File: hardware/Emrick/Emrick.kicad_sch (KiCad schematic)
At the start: 88 parts, among them J1 LED_STRIP_CONNECTOR, J2 UFL, J3 Conn_02x05_Odd_Even, J4 BATT_CONN, P1 USB_C_Plug_USB2.0, Q1 Q_NMOS_DGS, Q2 Q_NMOS_DGS, Q3 Q_NMOS_DGS, SW1 SW_SPST, SW2 SW_MEC_5E (RESET)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

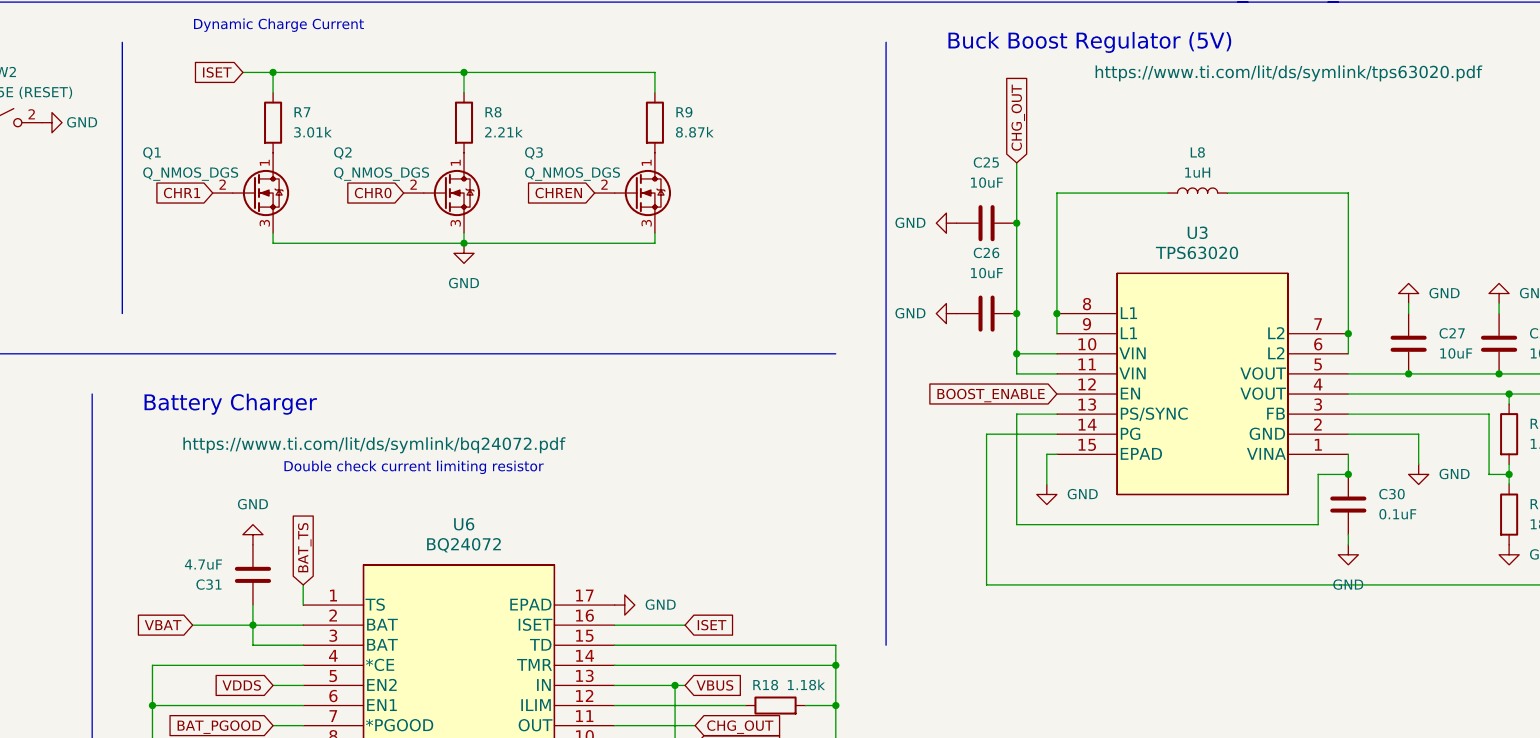
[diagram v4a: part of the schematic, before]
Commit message: switch NMOS to GSD and assign SOT-23 handsoldering footprint
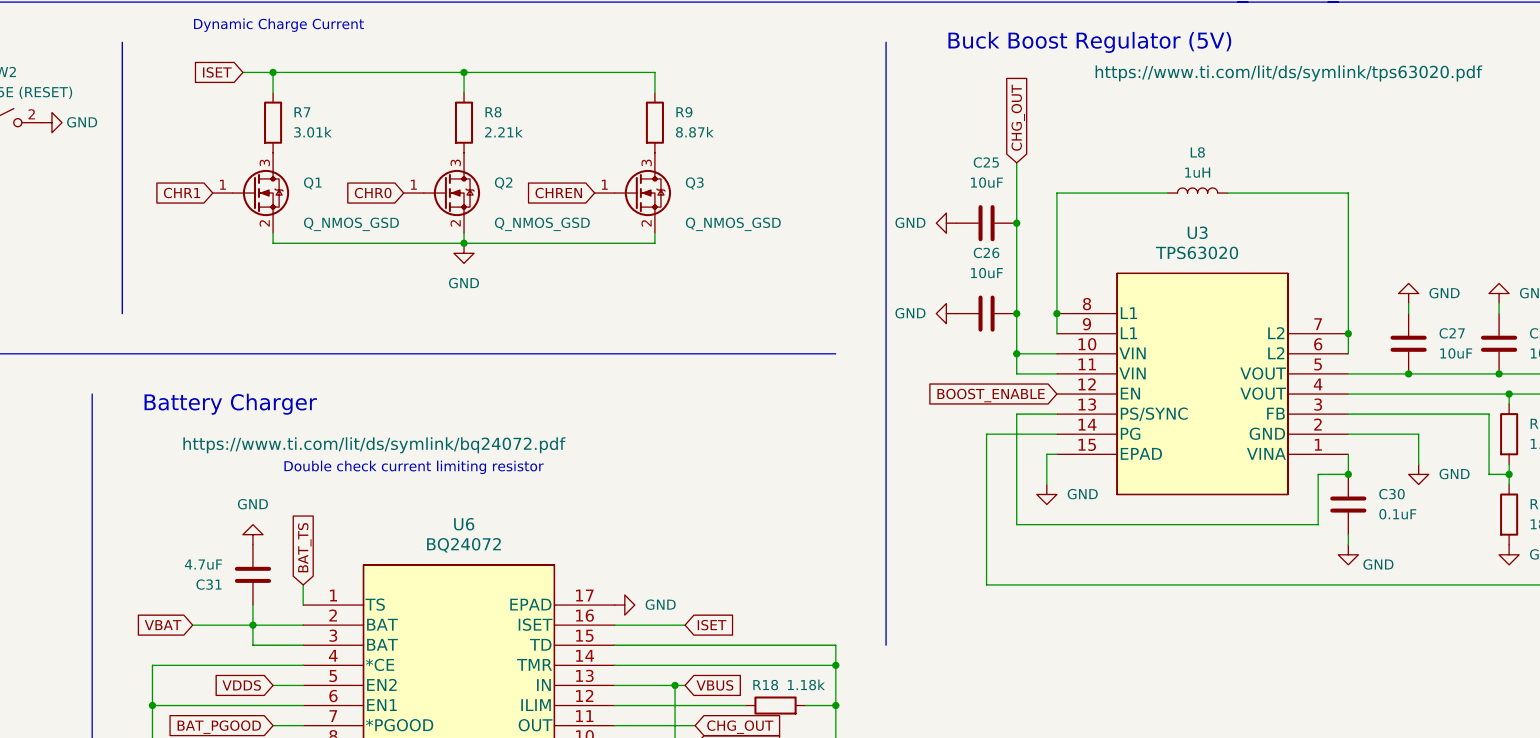
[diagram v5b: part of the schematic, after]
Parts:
- removed Q1, Q2, Q3: Q_NMOS_DGS, symbol Device:Q_NMOS_DGS
- added Q1, Q2, Q3: Q_NMOS_GSD, Package_TO_SOT_SMD:SOT-23_Handsoldering, symbol Device:Q_NMOS_GSD
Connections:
- net CHR0: now also Q2.1 (G)
- net CHR1: now also Q1.1 (G)
- net CHREN: now also Q3.1 (G)
- net GND: now also Q1.2 (S), Q2.2 (S), Q3.2 (S)
- net at R9.2: now also Q3.3 (D)
- net at R7.2: now also Q1.3 (D)
- net at R8.2: now also Q2.3 (D)
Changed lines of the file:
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@@
     (pin "2")
+  )
+  (symbol (lib_id "Device:Q_NMOS_GSD") (at 242.57 190.5 0) (unit 1)
+    (in_bom yes) (on_board yes)
+    (property "Reference" "Q2" (id 0) (at 248.92 189.2299 0)
+      (effects (font (size 1.27 1.27)) (justify left))
+    )
+    (property "Value" "Q_NMOS_GSD" (id 1) (at 248.92 194.31 0)
+      (effects (font (size 1.27 1.27)) (justify left))
+    )
+    (property "Footprint" "Package_TO_SOT_SMD:SOT-23_Handsoldering" (id 2) (at 247.65 187.96 0)
+      (effects (font (size 1.27 1.27)) hide)
+    )
+    (property "Datasheet" "~" (id 3) (at 242.57 190.5 0)
+      (effects (font (size 1.27 1.27)) hide)
+    )
+    (pin "1")
+    (pin "2")
+    (pin "3")
+  )
+  (symbol (lib_id "Device:Q_NMOS_GSD") (at 218.44 190.5 0) (unit 1)
+    (in_bom yes) (on_board yes)
+    (property "Reference" "Q1" (id 0) (at 224.79 189.2299 0)
+      (effects (font (size 1.27 1.27)) (justify left))
+    )
+    (property "Value" "Q_NMOS_GSD" (id 1) (at 224.79 194.31 0)
+      (effects (font (size 1.27 1.27)) (justify left))
+    )
+    (property "Footprint" "Package_TO_SOT_SMD:SOT-23_Handsoldering" (id 2) (at 223.52 187.96 0)
+      (effects (font (size 1.27 1.27)) hide)
+    )
+    (property "Datasheet" "~" (id 3) (at 218.44 190.5 0)
+      (effects (font (size 1.27 1.27)) hide)
+    )
+    (pin "1")
+    (pin "2")
+    (pin "3")
   )
   (symbol (lib_id "Device:FerriteBead") (at 336.55 36.83 90) (unit 1)
@@
     (pin "2")
   )
-  (symbol (lib_id "Device:Q_NMOS_DGS") (at 266.7 190.5 0) (unit 1)
-    (in_bom yes) (on_board yes)
-    (property "Reference" "Q3" (id 0) (at 252.73 185.42 0)
-      (effects (font (size 1.27 1.27)) (justify left))
-    )
-    (property "Value" "Q_NMOS_DGS" (id 1) (at 252.73 187.96 0)
-      (effects (font (size 1.27 1.27)) (justify left))
-    )
-    (property "Footprint" "" (id 2) (at 271.78 187.96 0)
-      (effects (font (size 1.27 1.27)) hide)
-    )
-    (property "Datasheet" "~" (id 3) (at 266.7 190.5 0)
-      (effects (font (size 1.27 1.27)) hide)
-    )
-    (pin "1")
-    (pin "2")
-    (pin "3")
-  )
   (symbol (lib_id "power:GND") (at 240.03 158.75 0) (unit 1)
     (in_bom yes) (on_board yes) (fields_autoplaced)
@@
     )
     (pin "1")
+  )
+  (symbol (lib_id "Device:Q_NMOS_GSD") (at 266.7 190.5 0) (unit 1)
+    (in_bom yes) (on_board yes)
+    (property "Reference" "Q3" (id 0) (at 273.05 189.2299 0)
+      (effects (font (size 1.27 1.27)) (justify left))
+    )
+    (property "Value" "Q_NMOS_GSD" (id 1) (at 273.05 194.31 0)
+      (effects (font (size 1.27 1.27)) (justify left))
+    )
+    (property "Footprint" "Package_TO_SOT_SMD:SOT-23_Handsoldering" (id 2) (at 271.78 187.96 0)
+      (effects (font (size 1.27 1.27)) hide)
+    )
+    (property "Datasheet" "~" (id 3) (at 266.7 190.5 0)
+      (effects (font (size 1.27 1.27)) hide)
+    )
+    (pin "1")
+    (pin "2")
+    (pin "3")
   )
   (symbol (lib_id "Device:Antenna") (at 339.09 113.03 0) (unit 1)
@@
     (pin "1")
     (pin "2")
-  )
-  (symbol (lib_id "Device:Q_NMOS_DGS") (at 242.57 190.5 0) (unit 1)
-    (in_bom yes) (on_board yes)
-    (property "Reference" "Q2" (id 0) (at 228.6 185.42 0)
-      (effects (font (size 1.27 1.27)) (justify left))
-    )
-    (property "Value" "Q_NMOS_DGS" (id 1) (at 228.6 187.96 0)
-      (effects (font (size 1.27 1.27)) (justify left))
-    )
-    (property "Footprint" "" (id 2) (at 247.65 187.96 0)
-      (effects (font (size 1.27 1.27)) hide)
-    )
-    (property "Datasheet" "~" (id 3) (at 242.57 190.5 0)
-      (effects (font (size 1.27 1.27)) hide)
-    )
-    (pin "1")
-    (pin "2")
-    (pin "3")
   )
   (symbol (lib_id "Device:C") (at 240.03 104.14 180) (unit 1)
@@
     (pin "2")
   )
-  (symbol (lib_id "Device:Q_NMOS_DGS") (at 218.44 190.5 0) (unit 1)
-    (in_bom yes) (on_board yes)
-    (property "Reference" "Q1" (id 0) (at 204.47 185.42 0)
-      (effects (font (size 1.27 1.27)) (justify left))
-    )
-    (property "Value" "Q_NMOS_DGS" (id 1) (at 204.47 187.96 0)
-      (effects (font (size 1.27 1.27)) (justify left))
-    )
-    (property "Footprint" "" (id 2) (at 223.52 187.96 0)
-      (effects (font (size 1.27 1.27)) hide)
-    )
-    (property "Datasheet" "~" (id 3) (at 218.44 190.5 0)
-      (effects (font (size 1.27 1.27)) hide)
-    )
-    (pin "1")
-    (pin "2")
-    (pin "3")
-  )
   (symbol (lib_id "Device:LED") (at 106.68 34.29 0) (unit 1)
     (in_bom yes) (on_board yes)
@@
   )
   (symbol (lib_id "power:GND") (at 356.87 234.95 0) (unit 1)
-    (in_bom yes) (on_board yes) (fields_autoplaced)
+    (in_bom yes) (on_board yes)
     (property "Reference" "#PWR039" (id 0) (at 356.87 241.3 0)
       (effects (font (size 1.27 1.27)) hide)
     )
-    (property "Value" "GND" (id 1) (at 356.87 240.03 0))
+    (property "Value" "GND" (id 1) (at 360.68 237.49 0))
     (property "Footprint" "" (id 2) (at 356.87 234.95 0)
       (effects (font (size 1.27 1.27)) hide)
@@
       (reference "P1") (unit 1) (value "USB_C_Plug_USB2.0") (footprint "Connector_USB:USB_C_Receptacle_XKB_U262-16XN-4BVC11")
     )
-    (path "/cb06ee6c-4b12-4bdb-8820-222eef2ada64"
-      (reference "Q1") (unit 1) (value "Q_NMOS_DGS") (footprint "")
-    )
-    (path "/8f86129a-1041-475e-83db-4a848e9888d9"
-      (reference "Q2") (unit 1) (value "Q_NMOS_DGS") (footprint "")
-    )
-    (path "/43d8ebd2-88bb-493c-bc4c-c7071928953f"
-      (reference "Q3") (unit 1) (value "Q_NMOS_DGS") (footprint "")
+    (path "/144ea137-bd73-4364-97c7-5aa60b624ac9"
+      (reference "Q1") (unit 1) (value "Q_NMOS_GSD") (footprint "Package_TO_SOT_SMD:SOT-23_Handsoldering")
+    )
+    (path "/144858b1-b791-41a4-b3af-8aa4ce7ea356"
+      (reference "Q2") (unit 1) (value "Q_NMOS_GSD") (footprint "Package_TO_SOT_SMD:SOT-23_Handsoldering")
+    )
+    (path "/56e0bbdb-5cd0-4cfa-80ba-ba3bf016e939"
+      (reference "Q3") (unit 1) (value "Q_NMOS_GSD") (footprint "Package_TO_SOT_SMD:SOT-23_Handsoldering")
     )
     (path "/7c976042-82e8-4bec-9beb-b8a292d80d1c"

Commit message: revision 2
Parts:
- C12: footprint Capacitor_SMD:C_0201_0603Metric -> Capacitor_SMD:C_0402_1005Metric
- C13: footprint Capacitor_SMD:C_0201_0603Metric -> Capacitor_SMD:C_0603_1608Metric
- C29: footprint Capacitor_SMD:C_0402_1005Metric -> Capacitor_SMD:C_0603_1608Metric
- L9: footprint Inductor_SMD:L_0402_1005Metric -> Capacitor_SMD:C_0603_1608Metric
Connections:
- net BOOST_ENABLE: now also U2.18 (DIO_12); no longer U2.29 (DIO_19)
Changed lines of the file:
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@@
   (junction (at 292.1 255.27) (diameter 0) (color 0 0 0 0)
   )
+  (no_connect (at 217.17 83.82))
   (no_connect (at 158.75 248.92))
   (no_connect (at 158.75 256.54))
@@
   (no_connect (at 62.23 40.64))
   (no_connect (at 217.17 63.5))
-  (no_connect (at 217.17 66.04))
+  (no_connect (at 217.17 88.9))
   (no_connect (at 217.17 38.1))
   (no_connect (at 217.17 91.44))
@@
   (no_connect (at 45.72 172.72))
   (no_connect (at 217.17 106.68))
-  (no_connect (at 217.17 88.9))
   (no_connect (at 217.17 104.14))
   (no_connect (at 217.17 101.6))
@@
     )
   )
-  (global_label "BOOST_ENABLE" (shape input) (at 217.17 83.82 0) (fields_autoplaced)
+  (global_label "BOOST_ENABLE" (shape input) (at 217.17 66.04 0) (fields_autoplaced)
     (effects (font (size 1.27 1.27)) (justify left))
-    (property "Intersheet References" "${INTERSHEET_REFS}" (id 0) (at 233.6741 83.7406 0)
+    (property "Intersheet References" "${INTERSHEET_REFS}" (id 0) (at 233.6741 65.9606 0)
       (effects (font (size 1.27 1.27)) (justify left) hide)
     )
@@
       (effects (font (size 1.27 1.27)) (justify left))
     )
-    (property "Footprint" "Inductor_SMD:L_0402_1005Metric" (id 2) (at 320.04 125.73 0)
+    (property "Footprint" "Capacitor_SMD:C_0603_1608Metric" (id 2) (at 320.04 125.73 0)
       (effects (font (size 1.27 1.27)) hide)
     )
@@
       (effects (font (size 1.27 1.27)) (justify left))
     )
-    (property "Footprint" "Capacitor_SMD:C_0201_0603Metric" (id 2) (at 287.9852 109.22 0)
+    (property "Footprint" "Capacitor_SMD:C_0402_1005Metric" (id 2) (at 287.9852 109.22 0)
       (effects (font (size 1.27 1.27)) hide)
     )
@@
       (effects (font (size 1.27 1.27)) (justify left))
     )
-    (property "Footprint" "Capacitor_SMD:C_0201_0603Metric" (id 2) (at 312.1152 129.54 0)
+    (property "Footprint" "Capacitor_SMD:C_0603_1608Metric" (id 2) (at 312.1152 129.54 0)
       (effects (font (size 1.27 1.27)) hide)
     )
@@
       (effects (font (size 1.27 1.27)) (justify right))
     )
-    (property "Footprint" "Capacitor_SMD:C_0402_1005Metric" (id 2) (at 386.3848 205.74 0)
+    (property "Footprint" "Capacitor_SMD:C_0603_1608Metric" (id 2) (at 386.3848 205.74 0)
       (effects (font (size 1.27 1.27)) hide)
     )
@@
     )
     (path "/4f3938ec-ee10-4033-b043-17e527f7cafe"
-      (reference "C12") (unit 1) (value "?") (footprint "Capacitor_SMD:C_0201_0603Metric")
+      (reference "C12") (unit 1) (value "?") (footprint "Capacitor_SMD:C_0402_1005Metric")
     )
     (path "/50c8f597-eecd-41b3-b369-057fd39f4039"
-      (reference "C13") (unit 1) (value "?") (footprint "Capacitor_SMD:C_0201_0603Metric")
+      (reference "C13") (unit 1) (value "?") (footprint "Capacitor_SMD:C_0603_1608Metric")
     )
     (path "/2b92eedf-d2a7-4ca6-a1c8-41794a417b5e"
@@
     )
     (path "/80b7865e-df93-429c-94a4-4f595f2b7920"
-      (reference "C29") (unit 1) (value "10uF") (footprint "Capacitor_SMD:C_0402_1005Metric")
+      (reference "C29") (unit 1) (value "10uF") (footprint "Capacitor_SMD:C_0603_1608Metric")
     )
     (path "/0c17f3c6-00d6-4552-8d5c-ffe417b95235"
@@
     )
     (path "/3240c5b7-b3f1-4039-96ce-b8816fd0780e"
-      (reference "L9") (unit 1) (value "?") (footprint "Inductor_SMD:L_0402_1005Metric")
+      (reference "L9") (unit 1) (value "?") (footprint "Capacitor_SMD:C_0603_1608Metric")
     )
     (path "/98b2397c-2d8e-4422-bb18-42d4b4daae2e"

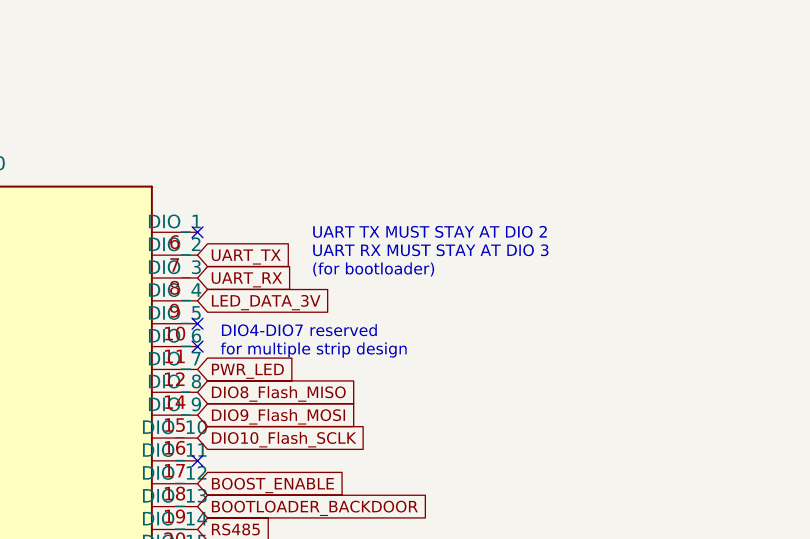
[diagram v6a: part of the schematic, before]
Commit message: update gerbers and uarttx on micro
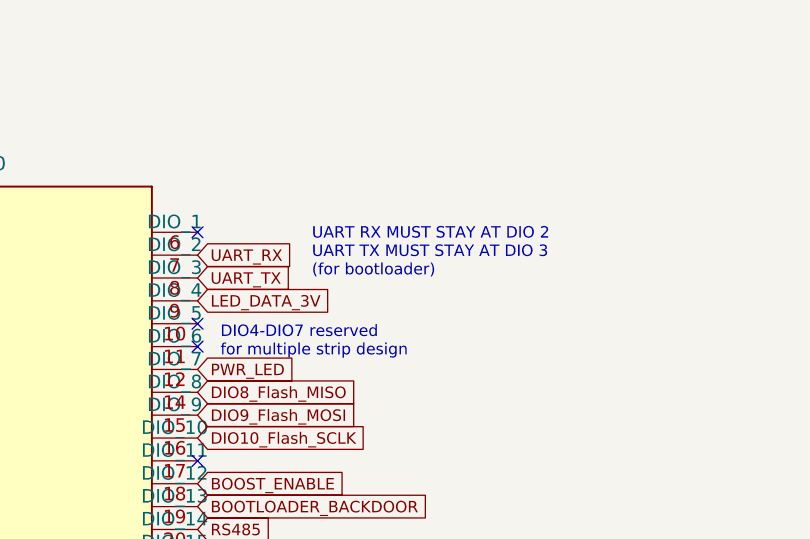
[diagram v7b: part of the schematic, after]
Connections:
- net UART_RX: now also U2.7 (DIO_2); no longer U2.8 (DIO_3)
- net UART_TX: now also U2.8 (DIO_3); no longer U2.7 (DIO_2)
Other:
- note added: "UART RX MUST STAY AT DIO 2 UART TX MUST STAY AT DIO 3 (for bootloader)"
- note removed: "UART TX MUST STAY AT DIO 2 UART RX MUST STAY AT DIO 3 (for bootloader)"
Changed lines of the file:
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@@
     (effects (font (size 1.27 1.27)) (justify left bottom))
   )
-  (text "UART TX MUST STAY AT DIO 2\nUART RX MUST STAY AT DIO 3\n(for bootloader)"
+  (text "UART RX MUST STAY AT DIO 2\nUART TX MUST STAY AT DIO 3\n(for bootloader)"
     (at 229.87 43.18 0)
     (effects (font (size 1.27 1.27)) (justify left bottom))
@@
     )
   )
-  (global_label "UART_TX" (shape input) (at 217.17 40.64 0) (fields_autoplaced)
-    (effects (font (size 1.27 1.27)) (justify left))
-    (property "Intersheet References" "${INTERSHEET_REFS}" (id 0) (at 227.3845 40.5606 0)
+  (global_label "UART_TX" (shape input) (at 217.17 43.18 0) (fields_autoplaced)
+    (effects (font (size 1.27 1.27)) (justify left))
+    (property "Intersheet References" "${INTERSHEET_REFS}" (id 0) (at 227.3845 43.1006 0)
       (effects (font (size 1.27 1.27)) (justify left) hide)
     )
@@
     )
   )
-  (global_label "UART_RX" (shape input) (at 217.17 43.18 0) (fields_autoplaced)
-    (effects (font (size 1.27 1.27)) (justify left))
-    (property "Intersheet References" "${INTERSHEET_REFS}" (id 0) (at 227.6869 43.1006 0)
-      (effects (font (size 1.27 1.27)) (justify left) hide)
-    )
+  (global_label "UART_RX" (shape input) (at 217.17 40.64 0) (fields_autoplaced)
+    (effects (font (size 1.27 1.27)) (justify left))
+    (property "Intersheet References" "${INTERSHEET_REFS}" (id 0) (at 227.6869 40.5606 0)
+      (effects (font (size 1.27 1.27)) (justify left) hide)
+    )
